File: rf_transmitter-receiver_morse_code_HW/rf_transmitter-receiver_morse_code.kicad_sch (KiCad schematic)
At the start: 8 parts, among them U1 SC09147

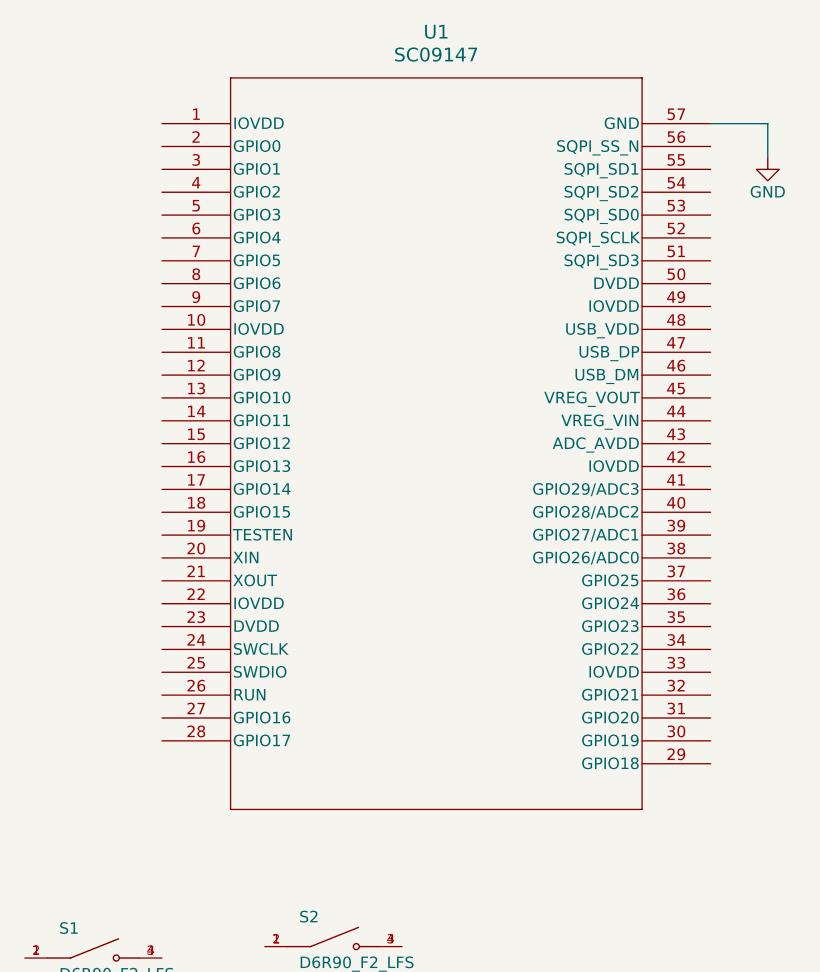
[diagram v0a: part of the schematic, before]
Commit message: Successful testing of button inputs keeping Serial Monitor capabilities in Arduino IDE, and engineering notes added for documentation process.
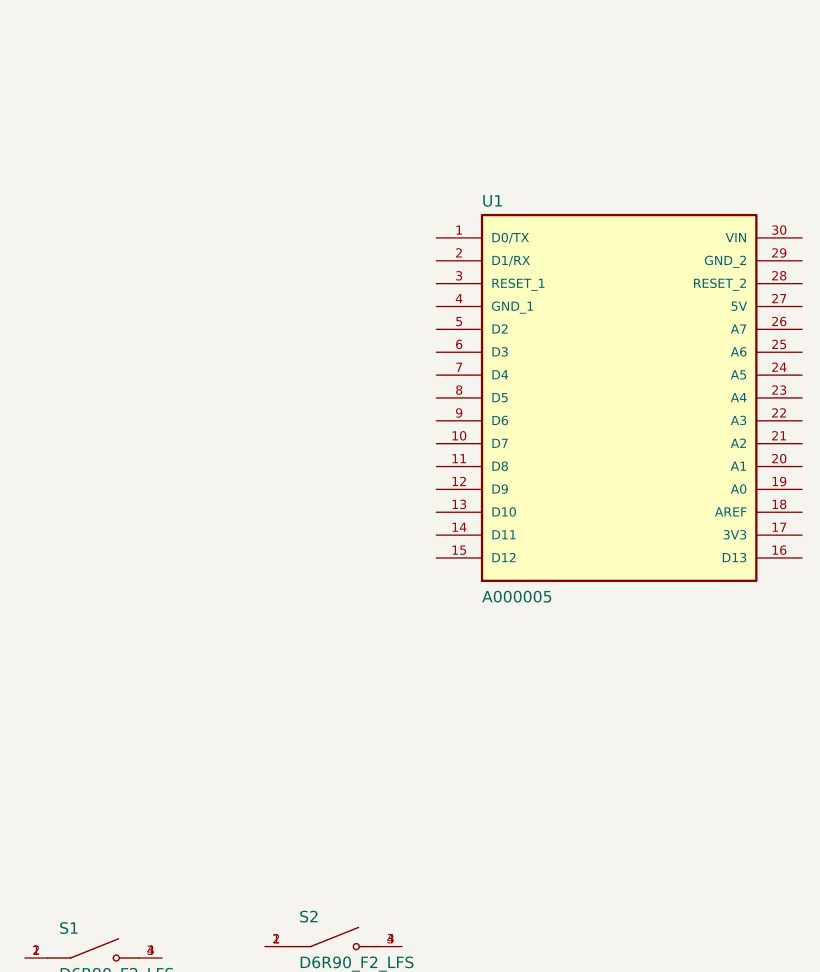
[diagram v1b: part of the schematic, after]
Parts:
- removed U1: SC09147, QFN56_7X7_RPI, symbol RP-2040:SC09147
- added U1: A000005, A000005:MODULE_A000005, symbol A000005:A000005

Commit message: Slight schematic updates?
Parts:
- removed D1, D2, D3, D4, D5: LTST-S270GKT, LTST-S270GKT:0603, symbol LTST-S270GKT:LTST-S270GKT
- added D? (x2): WL-SFTW_3528_PLCC4, WL-SFTW_3528_PLCC4:WL-SFTW_3528_PLCC4, symbol WL-SFTW_3528_PLCC4:WL-SFTW_3528_PLCC4
- added R1, R2, R? (x2): R, symbol Device:R
- added U2: MAX1472AKA+T, 21-0078H_MXM, symbol MAX1472AKA:MAX1472AKA+T
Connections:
- net at U1.10 (D7): now also D?.4
- net GND: now reaches U1.29 (GND_2)
- net GND: now also U1.4 (GND_1), R1.2, R2.2, U2.2 (GND), U2.3 (PAGND)
- net at U1.5 (D2): now also S1.3, S1.4, R2.1
- net at U1.6 (D3): now also S2.3, S2.4, R1.1
- net at U1.7 (D4): now also D?.2
- net at U1.8 (D5): now also D?.4
- net at U1.9 (D6): now also D?.2
- net +3.3V: now reaches S1.1, S1.2
- net +3.3V: now also S2.1, S2.2, R?.1, R?.1
- new net: D?.1, R?.2 (x2)
- new net VCC: U2.7 (VDD)
- no-connect marks 0 -> 2
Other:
- added sheet Receiver (Receiver.kicad_sch)
- moved on the sheet: S1, S2, U1
